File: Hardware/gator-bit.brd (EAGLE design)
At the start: 114.3 x 66 mm, 82 parts, among them J19 GATOR, J2 GATOR, J20 GATOR, J21 GATOR, J22 GATOR, J25 GATOR, J28 GATOR, J3 GATOR, J32 GATOR, J33 GATOR, J34 GATOR, J35 GATOR, J36 GATOR, J39 GATOR, J4 GATOR, J40 GATOR, U2 micro:bit, U4 MIC5219 3.3V

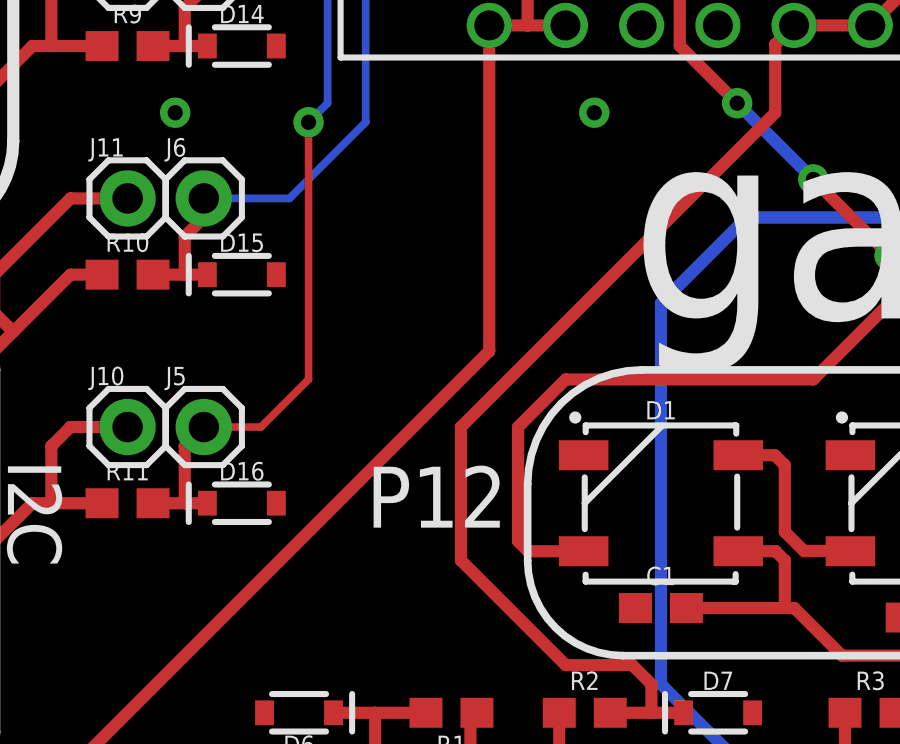
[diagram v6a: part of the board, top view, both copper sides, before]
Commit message: adding OSHW logo, VIN range note
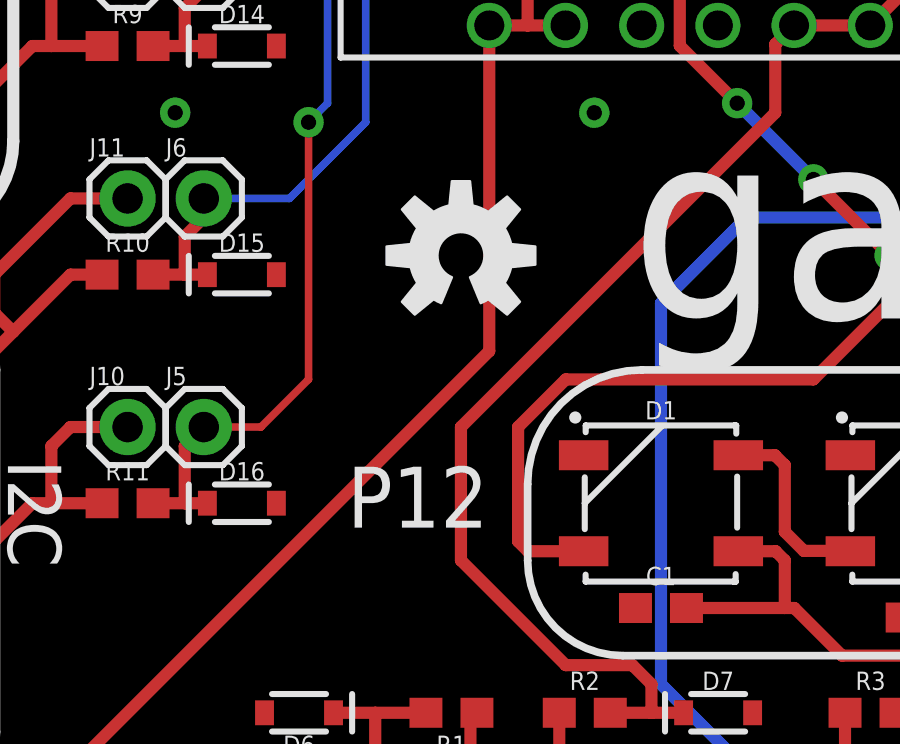
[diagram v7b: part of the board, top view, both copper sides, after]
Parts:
- added LOGO2: OSHW-LOGOM, SparkFun-Aesthetics:OSHW-LOGO-M
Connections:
- removed net P10: U2.A25
- removed net P3: U2.A40
- removed net P4: U2.A35
- removed net P6: U2.A33
- removed net P7: U2.A32
- removed net P9: U2.A26
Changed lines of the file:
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@@
 <text x="14.535125" y="50.46685625" size="1.778" layer="21" font="vector" ratio="15" rot="SR270">MISO</text>
 <text x="14.569234375" y="59.52904375" size="1.778" layer="21" font="vector" ratio="15" rot="SR270">SCK</text>
-<text x="29.54591875" y="24.586871875" size="2.032" layer="21" font="vector" ratio="15" rot="SR0">P12</text>
+<text x="28.91091875" y="24.586871875" size="2.032" layer="21" font="vector" ratio="15" rot="SR0">P12</text>
 <dimension x1="2.54" y1="2.54" x2="0" y2="2.54" x3="1.27" y3="-3.81" textsize="1.778" layer="47" unit="inch"/>
 <dimension x1="2.54" y1="63.5" x2="0" y2="63.5" x3="1.27" y3="74.93" textsize="1.778" layer="47" unit="inch"/>
@@
 <attribute name="PROD_ID" value="SWCH-08179" x="97.79" y="5.08" size="1.778" layer="27" rot="R270" display="off"/>
 </element>
+<element name="LOGO2" library="SparkFun-Aesthetics" package="OSHW-LOGO-M" value="OSHW-LOGOM" x="32.7025" y="33.655"/>
 </elements>
 <signals>
@@
 <wire x1="86.6775" y1="21.59" x2="86.6775" y2="18.415" width="0.4064" layer="1"/>
 </signal>
-<signal name="P10">
-<contactref element="U2" pad="A25"/>
-</signal>
-<signal name="P7">
-<contactref element="U2" pad="A32"/>
-</signal>
-<signal name="P6">
-<contactref element="U2" pad="A33"/>
-</signal>
 <signal name="P5">
 <contactref element="U2" pad="A34"/>
@@
 <wire x1="39.9962375" y1="43.227525" x2="39.9962375" y2="40.6487625" width="0.4064" layer="1"/>
 </signal>
-<signal name="P4">
-<contactref element="U2" pad="A35"/>
-</signal>
-<signal name="P3">
-<contactref element="U2" pad="A40"/>
-</signal>
-<signal name="P9">
-<contactref element="U2" pad="A26"/>
-</signal>
 <signal name="P0">

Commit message: updating resistor values
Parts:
- R1, R10, R11, R12, R13, R2, R3, R4, R5, R6, R8, R9: value 1k -> 2.0k
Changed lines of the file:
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@@
 <attribute name="PROD_ID" value="DIO-11284" x="27.305" y="18.415" size="1.778" layer="27" rot="R180" display="off"/>
 </element>
-<element name="R1" library="SparkFun-Resistors" package="0603" value="1k" x="32.385" y="18.415" rot="R180">
-<attribute name="PROD_ID" value="RES-07856" x="32.385" y="18.415" size="1.778" layer="27" rot="R180" display="off"/>
+<element name="R1" library="SparkFun-Resistors" package="0603" value="2.0k" x="32.385" y="18.415" rot="R180">
+<attribute name="PROD_ID" value="RES-08296" x="32.385" y="18.415" size="1.778" layer="27" rot="R180" display="off"/>
 </element>
 <element name="S2" library="SparkFun-Switches" package="SWITCH_DPDT_SMD_AYZ0202" value="" x="91.44" y="45.72">
@@
 <attribute name="PROD_ID" value="DIO-11284" x="41.275" y="22.225" size="1.778" layer="27" display="off"/>
 </element>
-<element name="R2" library="SparkFun-Resistors" package="0603" value="1k" x="36.83" y="18.415">
-<attribute name="PROD_ID" value="RES-07856" x="36.83" y="14.605" size="1.778" layer="27" display="off"/>
+<element name="R2" library="SparkFun-Resistors" package="0603" value="2.0k" x="36.83" y="18.415">
+<attribute name="PROD_ID" value="RES-08296" x="36.83" y="14.605" size="1.778" layer="27" display="off"/>
 </element>
 <element name="D8" library="SparkFun-DiscreteSemi" package="SOD-323" value="3.3V" x="50.8" y="18.415">
 <attribute name="PROD_ID" value="DIO-11284" x="50.8" y="22.225" size="1.778" layer="27" display="off"/>
 </element>
-<element name="R3" library="SparkFun-Resistors" package="0603" value="1k" x="46.355" y="18.415">
-<attribute name="PROD_ID" value="RES-07856" x="46.355" y="14.605" size="1.778" layer="27" display="off"/>
+<element name="R3" library="SparkFun-Resistors" package="0603" value="2.0k" x="46.355" y="18.415">
+<attribute name="PROD_ID" value="RES-08296" x="46.355" y="14.605" size="1.778" layer="27" display="off"/>
 </element>
 <element name="D9" library="SparkFun-DiscreteSemi" package="SOD-323" value="3.3V" x="80.01" y="18.415">
 <attribute name="PROD_ID" value="DIO-11284" x="73.66" y="26.035" size="1.778" layer="27" display="off"/>
 </element>
-<element name="R4" library="SparkFun-Resistors" package="0603" value="1k" x="75.565" y="18.415">
-<attribute name="PROD_ID" value="RES-07856" x="75.565" y="14.605" size="1.778" layer="27" display="off"/>
+<element name="R4" library="SparkFun-Resistors" package="0603" value="2.0k" x="75.565" y="18.415">
+<attribute name="PROD_ID" value="RES-08296" x="75.565" y="14.605" size="1.778" layer="27" display="off"/>
 </element>
 <element name="D10" library="SparkFun-DiscreteSemi" package="SOD-323" value="3.3V" x="89.535" y="18.415">
 <attribute name="PROD_ID" value="DIO-11284" x="89.535" y="22.225" size="1.778" layer="27" display="off"/>
 </element>
-<element name="R5" library="SparkFun-Resistors" package="0603" value="1k" x="84.455" y="18.415">
-<attribute name="PROD_ID" value="RES-07856" x="84.455" y="10.795" size="1.778" layer="27" display="off"/>
+<element name="R5" library="SparkFun-Resistors" package="0603" value="2.0k" x="84.455" y="18.415">
+<attribute name="PROD_ID" value="RES-08296" x="84.455" y="10.795" size="1.778" layer="27" display="off"/>
 </element>
 <element name="D11" library="SparkFun-DiscreteSemi" package="SOD-323" value="3.3V" x="25.4" y="57.15">
 <attribute name="PROD_ID" value="DIO-11284" x="21.59" y="53.34" size="1.778" layer="27" display="off"/>
 </element>
-<element name="R6" library="SparkFun-Resistors" package="0603" value="1k" x="21.59" y="57.15">
-<attribute name="PROD_ID" value="RES-07856" x="21.59" y="45.72" size="1.778" layer="27" display="off"/>
+<element name="R6" library="SparkFun-Resistors" package="0603" value="2.0k" x="21.59" y="57.15">
+<attribute name="PROD_ID" value="RES-08296" x="21.59" y="45.72" size="1.778" layer="27" display="off"/>
 </element>
 <element name="D13" library="SparkFun-DiscreteSemi" package="SOD-323" value="3.3V" x="25.4" y="48.26">
 <attribute name="PROD_ID" value="DIO-11284" x="25.4" y="52.07" size="1.778" layer="27" display="off"/>
 </element>
-<element name="R8" library="SparkFun-Resistors" package="0603" value="1k" x="21.59" y="48.26">
-<attribute name="PROD_ID" value="RES-07856" x="21.59" y="44.45" size="1.778" layer="27" display="off"/>
+<element name="R8" library="SparkFun-Resistors" package="0603" value="2.0k" x="21.59" y="48.26">
+<attribute name="PROD_ID" value="RES-08296" x="21.59" y="44.45" size="1.778" layer="27" display="off"/>
 </element>
 <element name="D14" library="SparkFun-DiscreteSemi" package="SOD-323" value="3.3V" x="25.4" y="40.64">
 <attribute name="PROD_ID" value="DIO-11284" x="25.4" y="48.26" size="1.778" layer="27" display="off"/>
 </element>
-<element name="R9" library="SparkFun-Resistors" package="0603" value="1k" x="21.59" y="40.64">
-<attribute name="PROD_ID" value="RES-07856" x="21.59" y="36.83" size="1.778" layer="27" display="off"/>
+<element name="R9" library="SparkFun-Resistors" package="0603" value="2.0k" x="21.59" y="40.64">
+<attribute name="PROD_ID" value="RES-08296" x="21.59" y="36.83" size="1.778" layer="27" display="off"/>
 </element>
 <element name="D15" library="SparkFun-DiscreteSemi" package="SOD-323" value="3.3V" x="25.4" y="33.02">
 <attribute name="PROD_ID" value="DIO-11284" x="21.59" y="33.02" size="1.778" layer="27" display="off"/>
 </element>
-<element name="R10" library="SparkFun-Resistors" package="0603" value="1k" x="21.59" y="33.02">
-<attribute name="PROD_ID" value="RES-07856" x="15.875" y="21.59" size="1.778" layer="27" display="off"/>
+<element name="R10" library="SparkFun-Resistors" package="0603" value="2.0k" x="21.59" y="33.02">
+<attribute name="PROD_ID" value="RES-08296" x="15.875" y="21.59" size="1.778" layer="27" display="off"/>
 </element>
 <element name="D16" library="SparkFun-DiscreteSemi" package="SOD-323" value="3.3V" x="25.4" y="25.4">
 <attribute name="PROD_ID" value="DIO-11284" x="17.78" y="17.78" size="1.778" layer="27" display="off"/>
 </element>
-<element name="R11" library="SparkFun-Resistors" package="0603" value="1k" x="21.59" y="25.4">
-<attribute name="PROD_ID" value="RES-07856" x="21.59" y="10.16" size="1.778" layer="27" display="off"/>
+<element name="R11" library="SparkFun-Resistors" package="0603" value="2.0k" x="21.59" y="25.4">
+<attribute name="PROD_ID" value="RES-08296" x="21.59" y="10.16" size="1.778" layer="27" display="off"/>
 </element>
 <element name="D17" library="SparkFun-DiscreteSemi" package="SOD-323" value="3.3V" x="60.325" y="18.415">
 <attribute name="PROD_ID" value="DIO-11284" x="60.325" y="6.985" size="1.778" layer="27" display="off"/>
 </element>
-<element name="R12" library="SparkFun-Resistors" package="0603" value="1k" x="55.88" y="18.415">
-<attribute name="PROD_ID" value="RES-07856" x="50.165" y="-4.445" size="1.778" layer="27" display="off"/>
+<element name="R12" library="SparkFun-Resistors" package="0603" value="2.0k" x="55.88" y="18.415">
+<attribute name="PROD_ID" value="RES-08296" x="50.165" y="-4.445" size="1.778" layer="27" display="off"/>
 </element>
 <element name="C1" library="SparkFun-Capacitors" package="0603" value="0.1uF" x="39.37" y="21.9075">
@@
 <attribute name="PROD_ID" value="DIO-11284" x="70.485" y="22.225" size="1.778" layer="27" display="off"/>
 </element>
-<element name="R13" library="SparkFun-Resistors" package="0603" value="1k" x="66.04" y="18.415">
-<attribute name="PROD_ID" value="RES-07856" x="66.04" y="14.605" size="1.778" layer="27" display="off"/>
+<element name="R13" library="SparkFun-Resistors" package="0603" value="2.0k" x="66.04" y="18.415">
+<attribute name="PROD_ID" value="RES-08296" x="66.04" y="14.605" size="1.778" layer="27" display="off"/>
 </element>
 <element name="U4" library="SparkFun-IC-Power" package="SOT23-5" value="MIC5219 3.3V" x="86.995" y="30.48">
